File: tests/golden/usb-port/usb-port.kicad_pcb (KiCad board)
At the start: 2 copper layers, 38 x 40 mm, 7 parts, among them J1 USB_MICRO_B, J2 CONN_BRK_1X04

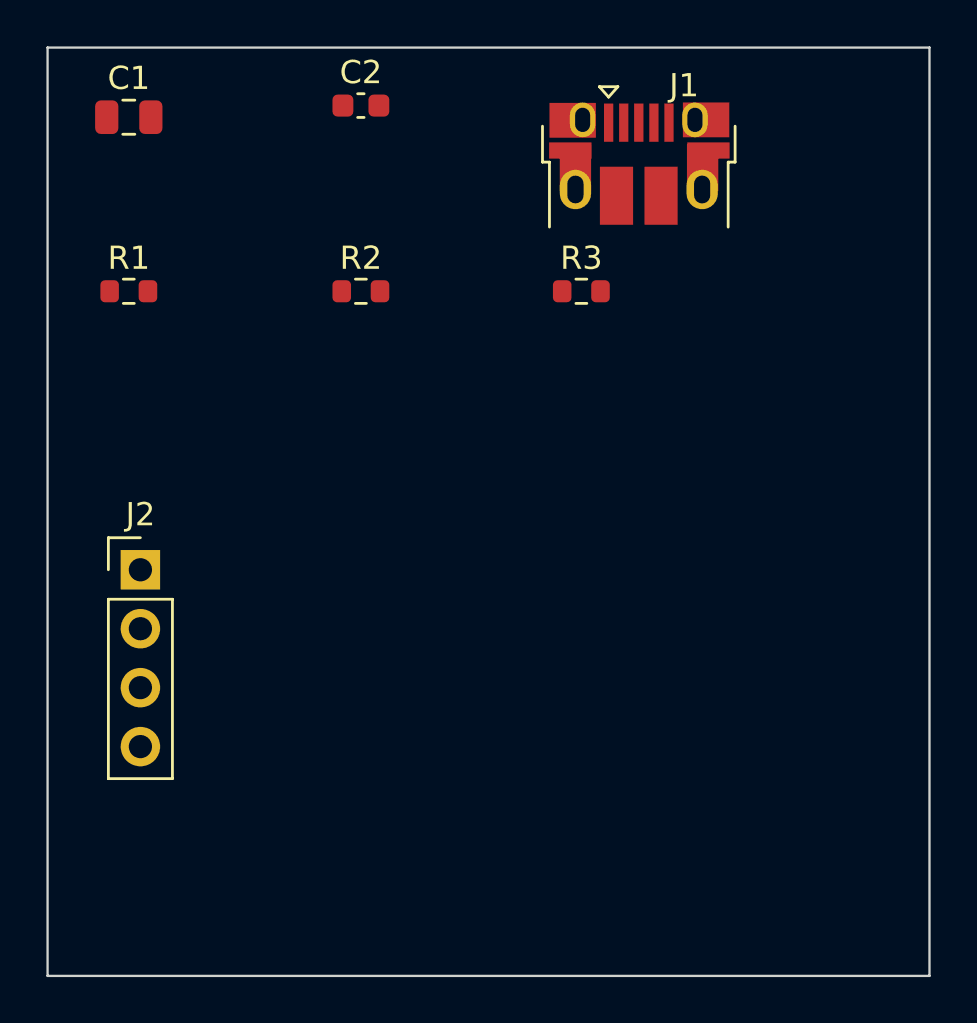
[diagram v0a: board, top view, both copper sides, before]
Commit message: M7a+M7b: topological routing — sketches in source, DRC-clean copper out
Routes are stored as topology: which obstacles a wire passes and on which side.
Nothing in the source is a coordinate, so moving a part leaves the sketch true and
only the tightening re-runs — which is the whole point of the approach (ADR 0006,
written after reading SURF, Maley, TopoR and the shortest-homotopic-path
literature).

Geometry comes from the classical pipeline: inflate obstacles by the clearance the
net needs, triangulate what is left (constrained Delaunay, via Shapely/GEOS), turn
the sketch into a crossing sequence, reduce it to a canonical homotopy class, and
tighten the resulting sleeve with the funnel algorithm. Inflating first is what
makes the shortest path automatically a legal one.

All four examples route with **zero DRC violations and zero schematic-parity
issues**; ldo-supply routes completely, 13 of 13 connections with nothing
unconnected. Unroutable connections are reported with a reason.

Almost every defect here was invisible to structural checks — the sleeve stayed
valid, the funnel still terminated, and the board was still legal. Each was found by
measuring the result:

* portal orientation had the wrong sign for Y-down board coordinates, turning a
  24.6 mm route into a 162.6 mm zigzag between the pad rows.
* searching triangle centroids instead of portal midpoints sent routes to the board
  corner and back, because a CDT of sparse obstacles has a few enormous triangles.
* an A* node has to be a *crossing*, not a diagonal: keyed on the diagonal alone the
  search steps through one without crossing it.
* feeding a finished route back as one convex hull swallowed the area inside every
  bend, costing a third of the connections.
* track obstacles pre-inflated by the routed net's own half-width left every later
  track short by half of its own, exactly as DRC reported.
* KiCad enforces the larger of two nets' clearances, not the routing net's.
* four shield tabs sharing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
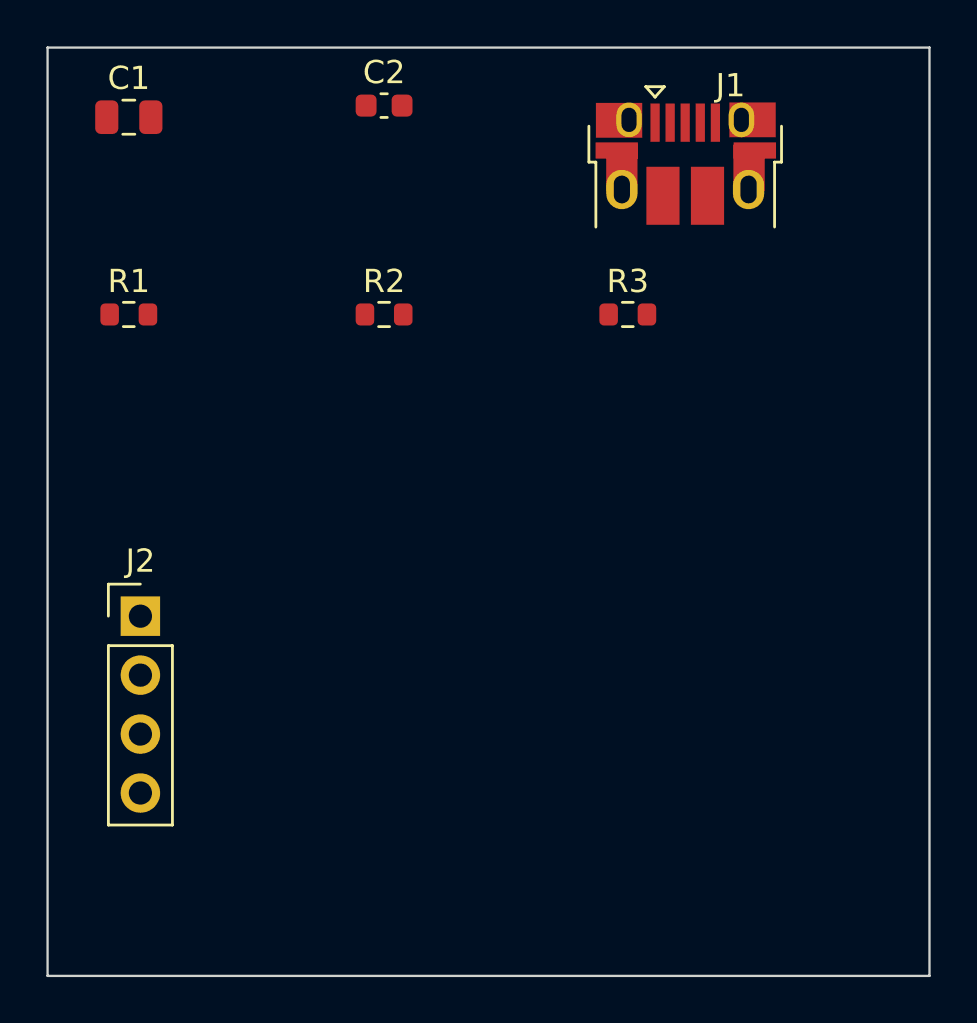
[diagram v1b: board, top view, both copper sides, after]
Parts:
- moved R3 2.24 mm to (125.0, 111.5)
- moved J1 2.00 mm to (127.5, 105.0)
- moved J2 2.00 mm to (104.0, 124.5)
- moved R2 1.41 mm to (114.5, 111.5)
- moved C2 1.00 mm to (114.5, 102.5)
- moved R1 1.00 mm to (103.5, 111.5)
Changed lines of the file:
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@@
 	(footprint "Capacitor_SMD:C_0603_1608Metric"
 		(layer "F.Cu")
-		(at 113.5 102.5 0)
+		(at 114.5 102.5 0)
 		(descr "Capacitor SMD 0603 (1608 Metric), square (rectangular) end terminal, IPC-7351 nominal, (Body size source: IPC-SM-782 page 76, https://www.pcb-3d.com/wordpress/wp-content/uploads/ipc-sm-782a_amendment_1_and_2.pdf), generated with kicad-footprint-generator")
 		(tags "capacitor")
@@
 	(footprint "Connector_USB:USB_Micro-B_Amphenol_10103594-0001LF_Horizontal"
 		(layer "F.Cu")
-		(at 125.5 105 0)
+		(at 127.5 105 0)
 		(descr "Micro USB Type B 10103594-0001LF, http://cdn.amphenol-icc.com/media/wysiwyg/files/drawing/10103594.pdf")
 		(tags "USB USB_B USB_micro USB_OTG")
@@
 	(footprint "Connector_PinHeader_2.54mm:PinHeader_1x04_P2.54mm_Vertical"
 		(layer "F.Cu")
-		(at 104 122.5 0)
+		(at 104 124.5 0)
 		(descr "Through hole straight pin header, 1x04, 2.54mm pitch, single row")
 		(tags "Through hole pin header THT 1x04 2.54mm single row")
@@
 	(footprint "Resistor_SMD:R_0603_1608Metric"
 		(layer "F.Cu")
-		(at 103.5 110.5 0)
+		(at 103.5 111.5 0)
 		(descr "Resistor SMD 0603 (1608 Metric), square (rectangular) end terminal, IPC-7351 nominal, (Body size source: IPC-SM-782 page 72, https://www.pcb-3d.com/wordpress/wp-content/uploads/ipc-sm-782a_amendment_1_and_2.pdf), generated with kicad-footprint-generator")
 		(tags "resistor")
@@
 	(footprint "Resistor_SMD:R_0603_1608Metric"
 		(layer "F.Cu")
-		(at 113.5 110.5 0)
+		(at 114.5 111.5 0)
 		(descr "Resistor SMD 0603 (1608 Metric), square (rectangular) end terminal, IPC-7351 nominal, (Body size source: IPC-SM-782 page 72, https://www.pcb-3d.com/wordpress/wp-content/uploads/ipc-sm-782a_amendment_1_and_2.pdf), generated with kicad-footprint-generator")
 		(tags "resistor")
@@
 	(footprint "Resistor_SMD:R_0603_1608Metric"
 		(layer "F.Cu")
-		(at 123 110.5 0)
+		(at 125 111.5 0)
 		(descr "Resistor SMD 0603 (1608 Metric), square (rectangular) end terminal, IPC-7351 nominal, (Body size source: IPC-SM-782 page 72, https://www.pcb-3d.com/wordpress/wp-content/uploads/ipc-sm-782a_amendment_1_and_2.pdf), generated with kicad-footprint-generator")
 		(tags "resistor")
